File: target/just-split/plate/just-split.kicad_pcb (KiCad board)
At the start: 2 copper layers, 128.2 x 112.4 mm, 0 parts

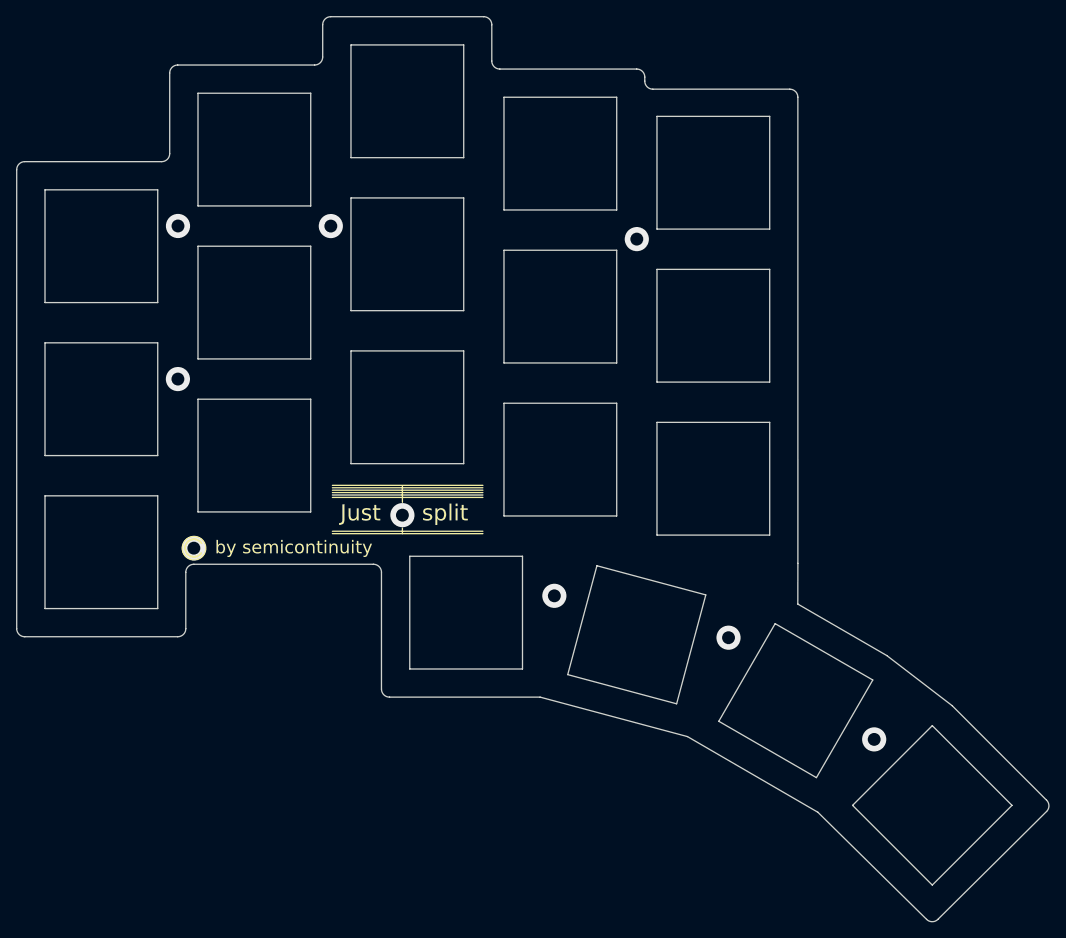
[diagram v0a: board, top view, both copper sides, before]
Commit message: just-split plate NPTH
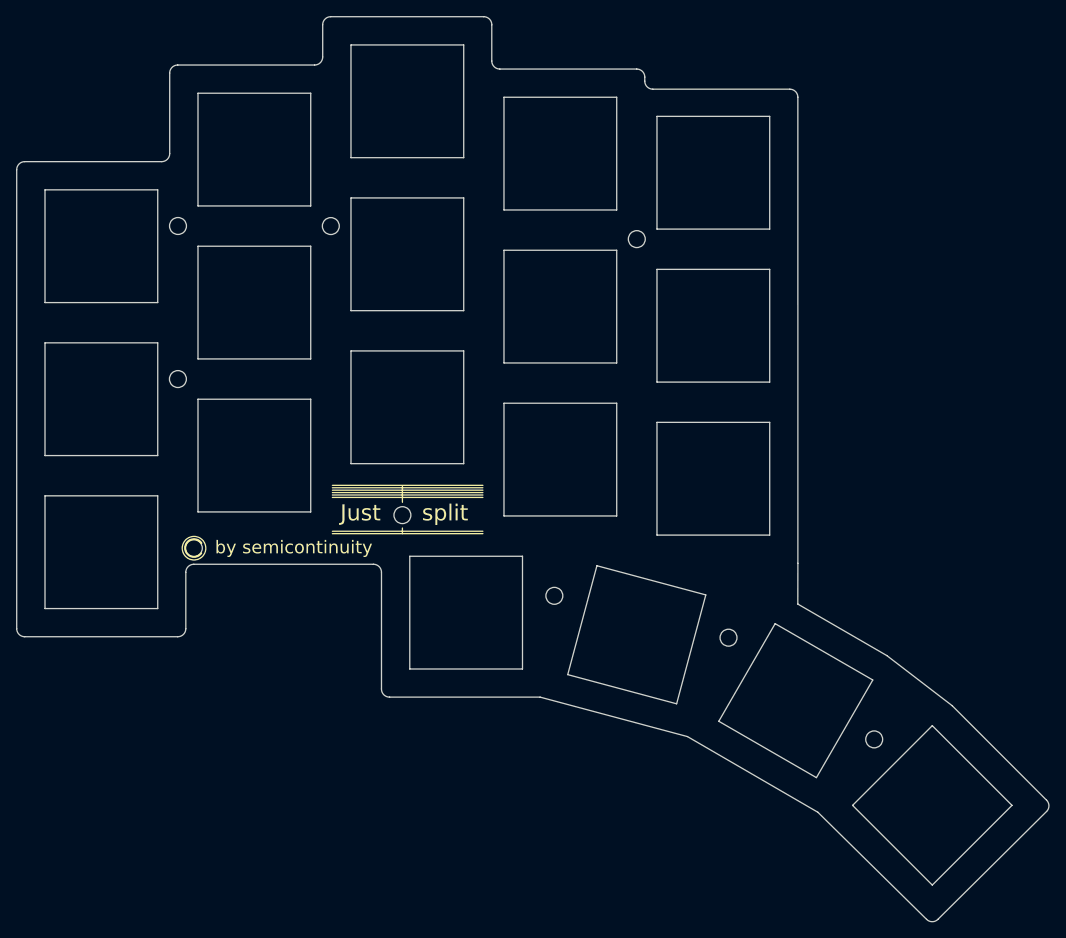
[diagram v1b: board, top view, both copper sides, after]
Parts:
- added REF**: MountingHole_2.1mm, MountingHole:MountingHole_2.1mm, F.Cu at (98.5, 100.4)
- added REF**: MountingHole_2.1mm, MountingHole:MountingHole_2.1mm, F.Cu at (126.4, 117.3)
- added REF**: MountingHole_2.1mm, MountingHole:MountingHole_2.1mm, F.Cu at (100.5, 121.4)
- added REF**: MountingHole_2.1mm, MountingHole:MountingHole_2.1mm, F.Cu at (98.5, 81.4)
- added REF**: MountingHole_2.1mm, MountingHole:MountingHole_2.1mm, F.Cu at (117.5, 81.4)
- added REF**: MountingHole_2.1mm, MountingHole:MountingHole_2.1mm, F.Cu at (155.5, 83.0)
- added REF**: MountingHole_2.1mm, MountingHole:MountingHole_2.1mm, F.Cu at (145.3, 127.3)
- added REF**: MountingHole_2.1mm, MountingHole:MountingHole_2.1mm, F.Cu at (166.9, 132.5)
- added REF**: MountingHole_2.1mm, MountingHole:MountingHole_2.1mm, F.Cu at (185.0, 145.1)
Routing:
- net (no net): vias 9 -> 0
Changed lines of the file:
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@@
     (thickness 1.6)
     (drawings 133)
-    (tracks 9)
+    (tracks 0)
     (zones 0)
-    (modules 0)
+    (modules 9)
     (nets 1)
   )
@@
     (46 B.CrtYd user hide)
     (47 F.CrtYd user hide)
-    (48 B.Fab user)
-    (49 F.Fab user)
+    (48 B.Fab user hide)
+    (49 F.Fab user hide)
   )
   (setup
@@
     (visible_elements FFFFF77F)
     (pcbplotparams
-      (layerselection 0x010f0_ffffffff)
+      (layerselection 0x010a0_7fffffff)
       (usegerberextensions true)
       (usegerberattributes false)
@@
       (psnegative false)
       (psa4output false)
-      (plotreference true)
-      (plotvalue true)
+      (plotreference false)
+      (plotvalue false)
       (plotinvisibletext false)
-      (padsonsilk false)
+      (padsonsilk true)
       (subtractmaskfromsilk true)
       (outputformat 1)
@@
     (uvia_dia 0.3)
     (uvia_drill 0.1)
+  )
+  (module MountingHole:MountingHole_2.1mm (layer F.Cu)
+    (at 98.50576 100.37278)
+    (descr "Mounting Hole 2.1mm, no annular")
+    (tags "mounting hole 2.1mm no annular")
+    (attr virtual)
+    (fp_text reference REF** (at 0 -3.2) (layer F.SilkS) hide
+      (effects (font (size 1 1) (thickness 0.15)))
+    )
+    (fp_text value MountingHole_2.1mm (at 0 3.2) (layer F.Fab) hide
+      (effects (font (size 1 1) (thickness 0.15)))
+    )
+    (fp_circle (center 0 0) (end 2.1 0) (layer Cmts.User) (width 0.15))
+    (fp_circle (center 0 0) (end 2.35 0) (layer F.CrtYd) (width 0.05))
+    (fp_text user %R (at 0.3 0) (layer F.Fab) hide
+      (effects (font (size 1 1) (thickness 0.15)))
+    )
+    (pad "" np_thru_hole circle (at 0 0) (size 2.1 2.1) (drill 2.1) (layers *.Cu *.Mask))
+  )
+  (module MountingHole:MountingHole_2.1mm (layer F.Cu)
+    (at 126.38576 117.27278)
+    (descr "Mounting Hole 2.1mm, no annular")
+    (tags "mounting hole 2.1mm no annular")
+    (attr virtual)
+    (fp_text reference REF** (at 0 -3.2) (layer F.SilkS) hide
+      (effects (font (size 1 1) (thickness 0.15)))
+    )
+    (fp_text value MountingHole_2.1mm (at 0 3.2) (layer F.Fab) hide
+      (effects (font (size 1 1) (thickness 0.15)))
+    )
+    (fp_circle (center 0 0) (end 2.1 0) (layer Cmts.User) (width 0.15))
+    (fp_circle (center 0 0) (end 2.35 0) (layer F.CrtYd) (width 0.05))
+    (fp_text user %R (at 0.3 0) (layer F.Fab) hide
+      (effects (font (size 1 1) (thickness 0.15)))
+    )
+    (pad "" np_thru_hole circle (at 0 0) (size 2.1 2.1) (drill 2.1) (layers *.Cu *.Mask))
+  )
+  (module MountingHole:MountingHole_2.1mm (layer F.Cu)
+    (at 100.48576 121.37278)
+    (descr "Mounting Hole 2.1mm, no annular")
+    (tags "mounting hole 2.1mm no annular")
+    (attr virtual)
+    (fp_text reference REF** (at 0 -3.2) (layer F.SilkS) hide
+      (effects (font (size 1 1) (thickness 0.15)))
+    )
+    (fp_text value MountingHole_2.1mm (at 0 3.2) (layer F.Fab) hide
+      (effects (font (size 1 1) (thickness 0.15)))
+    )
+    (fp_circle (center 0 0) (end 2.1 0) (layer Cmts.User) (width 0.15))
+    (fp_circle (center 0 0) (end 2.35 0) (layer F.CrtYd) (width 0.05))
+    (fp_text user %R (at 0.3 0) (layer F.Fab) hide
+      (effects (font (size 1 1) (thickness 0.15)))
+    )
+    (pad "" np_thru_hole circle (at 0 0) (size 2.1 2.1) (drill 2.1) (layers *.Cu *.Mask))
+  )
+  (module MountingHole:MountingHole_2.1mm (layer F.Cu)
+    (at 98.51576 81.36278)
+    (descr "Mounting Hole 2.1mm, no annular")
+    (tags "mounting hole 2.1mm no annular")
+    (attr virtual)
+    (fp_text reference REF** (at 0 -3.2) (layer F.SilkS) hide
+      (effects (font (size 1 1) (thickness 0.15)))
+    )
+    (fp_text value MountingHole_2.1mm (at 0 3.2) (layer F.Fab) hide
+      (effects (font (size 1 1) (thickness 0.15)))
+    )
+    (fp_circle (center 0 0) (end 2.1 0) (layer Cmts.User) (width 0.15))
+    (fp_circle (center 0 0) (end 2.35 0) (layer F.CrtYd) (width 0.05))
+    (fp_text user %R (at 0.3 0) (layer F.Fab) hide
+      (effects (font (size 1 1) (thickness 0.15)))
+    )
+    (pad "" np_thru_hole circle (at 0 0) (size 2.1 2.1) (drill 2.1) (layers *.Cu *.Mask))
+  )
+  (module MountingHole:MountingHole_2.1mm (layer F.Cu)
+    (at 117.49576 81.37278)
+    (descr "Mounting Hole 2.1mm, no annular")
+    (tags "mounting hole 2.1mm no annular")
+    (attr virtual)
+    (fp_text reference REF** (at 0 -3.2) (layer F.SilkS) hide
+      (effects (font (size 1 1) (thickness 0.15)))
+    )
+    (fp_text value MountingHole_2.1mm (at 0 3.2) (layer F.Fab) hide
+      (effects (font (size 1 1) (thickness 0.15)))
+    )
+    (fp_circle (center 0 0) (end 2.1 0) (layer Cmts.User) (width 0.15))
+    (fp_circle (center 0 0) (end 2.35 0) (layer F.CrtYd) (width 0.05))
+    (fp_text user %R (at 0.3 0) (layer F.Fab) hide
+      (effects (font (size 1 1) (thickness 0.15)))
+    )
+    (pad "" np_thru_hole circle (at 0 0) (size 2.1 2.1) (drill 2.1) (layers *.Cu *.Mask))
+  )
+  (module MountingHole:MountingHole_2.1mm (layer F.Cu)
+    (at 155.49576 82.99278)
+    (descr "Mounting Hole 2.1mm, no annular")
+    (tags "mounting hole 2.1mm no annular")
+    (attr virtual)
+    (fp_text reference REF** (at 0 -3.2) (layer F.SilkS) hide
+      (effects (font (size 1 1) (thickness 0.15)))
+    )
+    (fp_text value MountingHole_2.1mm (at 0 3.2) (layer F.Fab) hide
+      (effects (font (size 1 1) (thickness 0.15)))
+    )
+    (fp_circle (center 0 0) (end 2.1 0) (layer Cmts.User) (width 0.15))
+    (fp_circle (center 0 0) (end 2.35 0) (layer F.CrtYd) (width 0.05))
+    (fp_text user %R (at 0.3 0) (layer F.Fab) hide
+      (effects (font (size 1 1) (thickness 0.15)))
+    )
+    (pad "" np_thru_hole circle (at 0 0) (size 2.1 2.1) (drill 2.1) (layers *.Cu *.Mask))
+  )
+  (module MountingHole:MountingHole_2.1mm (layer F.Cu)
+    (at 145.25576 127.29278)
+    (descr "Mounting Hole 2.1mm, no annular")
+    (tags "mounting hole 2.1mm no annular")
+    (attr virtual)
+    (fp_text reference REF** (at 0 -3.2) (layer F.SilkS) hide
+      (effects (font (size 1 1) (thickness 0.15)))
+    )
+    (fp_text value MountingHole_2.1mm (at 0 3.2) (layer F.Fab) hide
+      (effects (font (size 1 1) (thickness 0.15)))
+    )
+    (fp_circle (center 0 0) (end 2.1 0) (layer Cmts.User) (width 0.15))
+    (fp_circle (center 0 0) (end 2.35 0) (layer F.CrtYd) (width 0.05))
+    (fp_text user %R (at 0.3 0) (layer F.Fab) hide
+      (effects (font (size 1 1) (thickness 0.15)))
+    )
+    (pad "" np_thru_hole circle (at 0 0) (size 2.1 2.1) (drill 2.1) (layers *.Cu *.Mask))
+  )
+  (module MountingHole:MountingHole_2.1mm (layer F.Cu)
+    (at 166.88576 132.49278)
+    (descr "Mounting Hole 2.1mm, no annular")
+    (tags "mounting hole 2.1mm no annular")
+    (attr virtual)
+    (fp_text reference REF** (at 0 -3.2) (layer F.SilkS) hide
+      (effects (font (size 1 1) (thickness 0.15)))
+    )
+    (fp_text value MountingHole_2.1mm (at 0 3.2) (layer F.Fab) hide
+      (effects (font (size 1 1) (thickness 0.15)))
+    )
+    (fp_circle (center 0 0) (end 2.1 0) (layer Cmts.User) (width 0.15))
+    (fp_circle (center 0 0) (end 2.35 0) (layer F.CrtYd) (width 0.05))
+    (fp_text user %R (at 0.3 0) (layer F.Fab) hide
+      (effects (font (size 1 1) (thickness 0.15)))
+    )
+    (pad "" np_thru_hole circle (at 0 0) (size 2.1 2.1) (drill 2.1) (layers *.Cu *.Mask))
+  )
+  (module MountingHole:MountingHole_2.1mm (layer F.Cu)
+    (at 184.97576 145.12278)
+    (descr "Mounting Hole 2.1mm, no annular")
+    (tags "mounting hole 2.1mm no annular")
+    (attr virtual)
+    (fp_text reference REF** (at 0 -3.2) (layer F.SilkS) hide
+      (effects (font (size 1 1) (thickness 0.15)))
+    )
+    (fp_text value MountingHole_2.1mm (at 0 3.2) (layer F.Fab) hide
+      (effects (font (size 1 1) (thickness 0.15)))
+    )
+    (fp_text user %R (at 0.3 0) (layer F.Fab) hide
+      (effects (font (size 1 1) (thickness 0.15)))
+    )
+    (fp_circle (center 0 0) (end 2.1 0) (layer Cmts.User) (width 0.15))
+    (fp_circle (center 0 0) (end 2.35 0) (layer F.CrtYd) (width 0.05))
+    (pad "" np_thru_hole circle (at 0 0) (size 2.1 2.1) (drill 2.1) (layers *.Cu *.Mask))
   )
   (gr_line (start 175.49 128.315) (end 175.5 123.255) (layer Edge.Cuts) (width 0.15))
@@
   (gr_arc (start 96.48576 72.37278) (end 96.48576 73.37278) (angle -90) (layer Edge.Cuts) (width 0.15))
   (gr_arc (start 79.48576 74.37278) (end 79.48576 73.37278) (angle -90) (layer Edge.Cuts) (width 0.15))
-  (via (at 166.88576 132.49278) (size 3) (drill 1.6) (layers F.Cu B.Cu) (net 0))
-  (via (at 184.97576 145.12278) (size 3) (drill 1.6) (layers F.Cu B.Cu) (net 0))
-  (via (at 145.25576 127.29278) (size 3) (drill 1.6) (layers F.Cu B.Cu) (net 0))
-  (via (at 98.50576 100.37278) (size 3) (drill 1.6) (layers F.Cu B.Cu) (net 0))
-  (via (at 100.48576 121.37278) (size 3) (drill 1.6) (layers F.Cu B.Cu) (net 0))
-  (via (at 117.49576 81.37278) (size 3) (drill 1.6) (layers F.Cu B.Cu) (net 0))
-  (via (at 126.38576 117.27278) (size 3) (drill 1.6) (layers F.Cu B.Cu) (net 0))
-  (via (at 98.51576 81.36278) (size 3) (drill 1.6) (layers F.Cu B.Cu) (net 0))
-  (via (at 155.49576 82.99278) (size 3) (drill 1.6) (layers F.Cu B.Cu) (net 0))
 )
